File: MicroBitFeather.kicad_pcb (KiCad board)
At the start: 2 copper layers, 67.3 x 35.6 mm, 16 parts, among them J1 Feather_Long, J2 Barrel_Jack_MountingPin, J3 Feather_Short, J4 NeoPixels, J5 microbit_edge_connector, U1 74AHCT125, U2 MCP1702-3302E_TO92

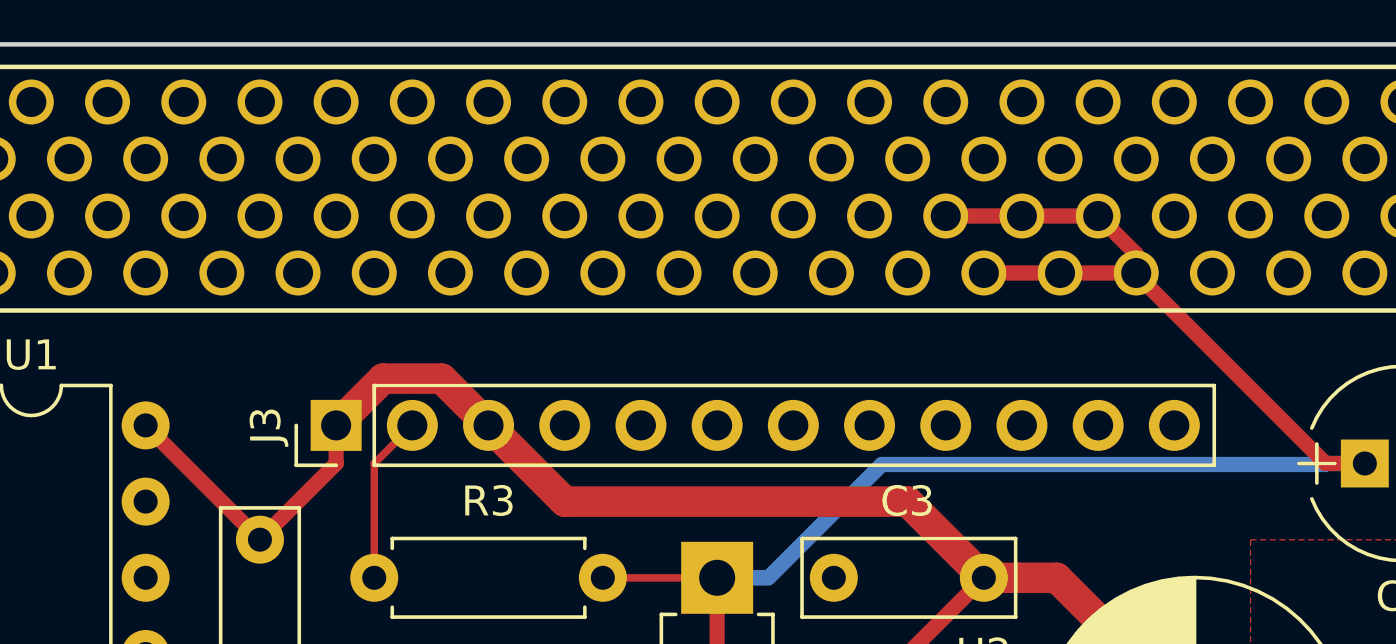
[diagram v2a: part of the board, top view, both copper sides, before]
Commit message: Some more tracks.
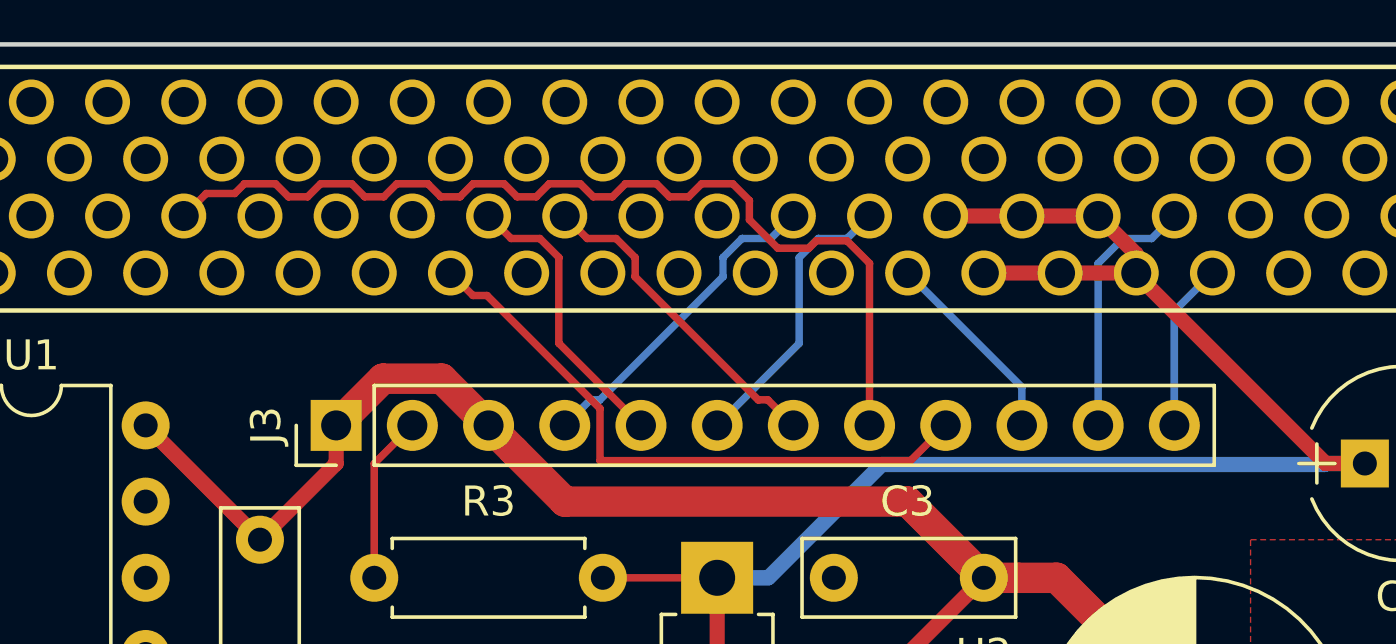
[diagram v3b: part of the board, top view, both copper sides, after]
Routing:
- net /P5: track 0.00 -> 32.6 mm
- net /P8: track 0.00 -> 20.6 mm
- net /SCK: track 0.00 -> 10.9 mm
- net /P11: track 0.00 -> 10.9 mm
- net /P9: track 0.00 -> 9.65 mm
- net /MOSI: track 0.00 -> 9.65 mm
- net /SCL: track 0.00 -> 8.60 mm
- net /P16: track 0.00 -> 6.66 mm
- net /SDA: track 0.00 -> 5.61 mm
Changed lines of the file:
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@@
     (thickness 1.6)
     (drawings 12)
-    (tracks 48)
+    (tracks 122)
     (zones 0)
     (modules 16)
@@
   )
   (setup
-    (last_trace_width 0.508)
+    (last_trace_width 0.25)
     (user_trace_width 0.508)
     (user_trace_width 1.016)
@@
   (segment (start 128.584999 112.885001) (end 125.73 115.74) (width 0.25) (layer F.Cu) (net 5))
   (segment (start 125.73 115.74) (end 125.73 116.84) (width 0.25) (layer F.Cu) (net 5))
+  (segment (start 143.51 96.52) (end 144.359999 95.670001) (width 0.25) (layer B.Cu) (net 13))
+  (segment (start 144.359999 95.670001) (end 144.681001 95.670001) (width 0.25) (layer B.Cu) (net 13))
+  (segment (start 144.681001 95.670001) (end 148.784999 91.566003) (width 0.25) (layer B.Cu) (net 13))
+  (segment (start 148.784999 91.566003) (end 148.784999 90.923999) (width 0.25) (layer B.Cu) (net 13))
+  (segment (start 148.784999 90.923999) (end 149.418999 90.289999) (width 0.25) (layer B.Cu) (net 13))
+  (segment (start 149.418999 90.289999) (end 150.380001 90.289999) (width 0.25) (layer B.Cu) (net 13))
+  (segment (start 150.380001 90.289999) (end 151.13 89.54) (width 0.25) (layer B.Cu) (net 13))
+  (segment (start 148.59 96.52) (end 151.324999 93.785001) (width 0.25) (layer B.Cu) (net 14))
+  (segment (start 151.324999 93.785001) (end 151.324999 90.923999) (width 0.25) (layer B.Cu) (net 14))
+  (segment (start 151.324999 90.923999) (end 151.958999 90.289999) (width 0.25) (layer B.Cu) (net 14))
+  (segment (start 151.958999 90.289999) (end 152.920001 90.289999) (width 0.25) (layer B.Cu) (net 14))
+  (segment (start 152.920001 90.289999) (end 153.67 89.54) (width 0.25) (layer B.Cu) (net 14))
   (segment (start 137.16 101.6) (end 137.16 97.79) (width 0.25) (layer F.Cu) (net 19))
   (segment (start 137.16 97.79) (end 138.43 96.52) (width 0.25) (layer F.Cu) (net 19))
+  (segment (start 146.05 96.52) (end 143.315001 93.785001) (width 0.25) (layer F.Cu) (net 20))
+  (segment (start 143.315001 93.785001) (end 143.315001 90.923999) (width 0.25) (layer F.Cu) (net 20))
+  (segment (start 143.315001 90.923999) (end 142.681001 90.289999) (width 0.25) (layer F.Cu) (net 20))
+  (segment (start 142.681001 90.289999) (end 141.719999 90.289999) (width 0.25) (layer F.Cu) (net 20))
+  (segment (start 141.719999 90.289999) (end 140.97 89.54) (width 0.25) (layer F.Cu) (net 20))
+  (segment (start 151.13 96.52) (end 150.280001 95.670001) (width 0.25) (layer F.Cu) (net 21))
+  (segment (start 150.280001 95.670001) (end 149.958999 95.670001) (width 0.25) (layer F.Cu) (net 21))
+  (segment (start 149.958999 95.670001) (end 145.855001 91.566003) (width 0.25) (layer F.Cu) (net 21))
+  (segment (start 145.855001 91.566003) (end 145.855001 90.923999) (width 0.25) (layer F.Cu) (net 21))
+  (segment (start 145.855001 90.923999) (end 145.221001 90.289999) (width 0.25) (layer F.Cu) (net 21))
+  (segment (start 145.221001 90.289999) (end 144.259999 90.289999) (width 0.25) (layer F.Cu) (net 21))
+  (segment (start 144.259999 90.289999) (end 143.51 89.54) (width 0.25) (layer F.Cu) (net 21))
+  (segment (start 153.67 96.52) (end 153.67 91.118998) (width 0.25) (layer F.Cu) (net 22))
+  (segment (start 153.67 91.118998) (end 152.916001 90.364999) (width 0.25) (layer F.Cu) (net 22))
+  (segment (start 151.896003 90.364999) (end 151.646001 90.615001) (width 0.25) (layer F.Cu) (net 22))
+  (segment (start 151.646001 90.615001) (end 150.613999 90.615001) (width 0.25) (layer F.Cu) (net 22))
+  (segment (start 152.916001 90.364999) (end 151.896003 90.364999) (width 0.25) (layer F.Cu) (net 22))
+  (segment (start 149.665001 89.666003) (end 149.665001 89.023999) (width 0.25) (layer F.Cu) (net 22))
+  (segment (start 150.613999 90.615001) (end 149.665001 89.666003) (width 0.25) (layer F.Cu) (net 22))
+  (segment (start 149.665001 89.023999) (end 149.106001 88.464999) (width 0.25) (layer F.Cu) (net 22))
+  (segment (start 149.106001 88.464999) (end 148.073999 88.464999) (width 0.25) (layer F.Cu) (net 22))
+  (segment (start 147.638998 88.9) (end 147.001002 88.9) (width 0.25) (layer F.Cu) (net 22))
+  (segment (start 148.073999 88.464999) (end 147.638998 88.9) (width 0.25) (layer F.Cu) (net 22))
+  (segment (start 146.566001 88.464999) (end 145.533999 88.464999) (width 0.25) (layer F.Cu) (net 22))
+  (segment (start 145.533999 88.464999) (end 145.098998 88.9) (width 0.25) (layer F.Cu) (net 22))
+  (segment (start 145.098998 88.9) (end 144.461002 88.9) (width 0.25) (layer F.Cu) (net 22))
+  (segment (start 147.001002 88.9) (end 146.566001 88.464999) (width 0.25) (layer F.Cu) (net 22))
+  (segment (start 144.461002 88.9) (end 144.026001 88.464999) (width 0.25) (layer F.Cu) (net 22))
+  (segment (start 144.026001 88.464999) (end 142.993999 88.464999) (width 0.25) (layer F.Cu) (net 22))
+  (segment (start 142.558998 88.9) (end 141.921002 88.9) (width 0.25) (layer F.Cu) (net 22))
+  (segment (start 142.993999 88.464999) (end 142.558998 88.9) (width 0.25) (layer F.Cu) (net 22))
+  (segment (start 141.486001 88.464999) (end 140.453999 88.464999) (width 0.25) (layer F.Cu) (net 22))
+  (segment (start 141.921002 88.9) (end 141.486001 88.464999) (width 0.25) (layer F.Cu) (net 22))
+  (segment (start 140.453999 88.464999) (end 140.018998 88.9) (width 0.25) (layer F.Cu) (net 22))
+  (segment (start 138.946001 88.464999) (end 137.913999 88.464999) (width 0.25) (layer F.Cu) (net 22))
+  (segment (start 139.381002 88.9) (end 138.946001 88.464999) (width 0.25) (layer F.Cu) (net 22))
+  (segment (start 140.018998 88.9) (end 139.381002 88.9) (width 0.25) (layer F.Cu) (net 22))
+  (segment (start 137.913999 88.464999) (end 137.478998 88.9) (width 0.25) (layer F.Cu) (net 22))
+  (segment (start 137.478998 88.9) (end 136.841002 88.9) (width 0.25) (layer F.Cu) (net 22))
+  (segment (start 136.406001 88.464999) (end 135.373999 88.464999) (width 0.25) (layer F.Cu) (net 22))
+  (segment (start 136.841002 88.9) (end 136.406001 88.464999) (width 0.25) (layer F.Cu) (net 22))
+  (segment (start 135.373999 88.464999) (end 134.938998 88.9) (width 0.25) (layer F.Cu) (net 22))
+  (segment (start 134.938998 88.9) (end 134.301002 88.9) (width 0.25) (layer F.Cu) (net 22))
+  (segment (start 134.301002 88.9) (end 133.866001 88.464999) (width 0.25) (layer F.Cu) (net 22))
+  (segment (start 133.866001 88.464999) (end 132.833999 88.464999) (width 0.25) (layer F.Cu) (net 22))
+  (segment (start 132.833999 88.464999) (end 132.508997 88.790001) (width 0.25) (layer F.Cu) (net 22))
+  (segment (start 132.508997 88.790001) (end 131.559999 88.790001) (width 0.25) (layer F.Cu) (net 22))
+  (segment (start 131.559999 88.790001) (end 130.81 89.54) (width 0.25) (layer F.Cu) (net 22))
+  (segment (start 156.21 96.52) (end 155.034999 97.695001) (width 0.25) (layer F.Cu) (net 23))
+  (segment (start 155.034999 97.695001) (end 144.685001 97.695001) (width 0.25) (layer F.Cu) (net 23))
+  (segment (start 144.685001 95.955999) (end 140.919001 92.189999) (width 0.25) (layer F.Cu) (net 23))
+  (segment (start 144.685001 97.695001) (end 144.685001 95.955999) (width 0.25) (layer F.Cu) (net 23))
+  (segment (start 140.919001 92.189999) (end 140.449999 92.189999) (width 0.25) (layer F.Cu) (net 23))
+  (segment (start 140.449999 92.189999) (end 139.7 91.44) (width 0.25) (layer F.Cu) (net 23))
+  (segment (start 158.75 96.52) (end 158.75 95.25) (width 0.25) (layer B.Cu) (net 24))
+  (segment (start 158.75 95.25) (end 154.94 91.44) (width 0.25) (layer B.Cu) (net 24))
+  (segment (start 161.29 96.52) (end 161.29 91.118998) (width 0.25) (layer B.Cu) (net 25))
+  (segment (start 161.29 91.118998) (end 162.118999 90.289999) (width 0.25) (layer B.Cu) (net 25))
+  (segment (start 162.118999 90.289999) (end 163.080001 90.289999) (width 0.25) (layer B.Cu) (net 25))
+  (segment (start 163.080001 90.289999) (end 163.83 89.54) (width 0.25) (layer B.Cu) (net 25))
+  (segment (start 163.83 96.52) (end 163.83 92.71) (width 0.25) (layer B.Cu) (net 26))
+  (segment (start 163.83 92.71) (end 165.1 91.44) (width 0.25) (layer B.Cu) (net 26))
   (zone (net 1) (net_name +5V) (layer F.Cu) (hatch edge 0.508)
     (connect_pads (clearance 0.3048))

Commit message: I meant for NeoPixel pin to be P0.
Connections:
- U1 pad 2: /P1 -> /P0
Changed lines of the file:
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@@
   (general
     (links 79)
-    (no_connects 71)
-    (area 115.424999 71.584999 217.260002 148.48)
+    (no_connects 50)
+    (area 118.034999 83.744999 185.495001 119.455001)
     (thickness 1.6)
     (drawings 12)
@@
       (net 69 "Net-(U1-Pad8)"))
     (pad 2 thru_hole oval (at 0 2.54) (size 1.6 1.6) (drill 0.8) (layers *.Cu *.Mask)
-      (net 8 /P1))
+      (net 7 /P0))
     (pad 9 thru_hole oval (at 7.62 12.7) (size 1.6 1.6) (drill 0.8) (layers *.Cu *.Mask)
       (net 2 GND))

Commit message: More tracks.
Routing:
- net /P3: track 0.00 -> 52.7 mm
- net /P0: track 0.00 -> 51.1 mm
- net /P4: track 0.00 -> 44.1 mm
- net /P2: track 0.00 -> 36.6 mm
- net /P1: track 0.00 -> 35.0 mm
- net /P10: track 0.00 -> 28.3 mm, vias 0 -> 2
- net /MOSI: track 9.65 -> 34.7 mm
- net /SCK: track 10.9 -> 34.8 mm, vias 0 -> 2
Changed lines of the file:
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@@
     (thickness 1.6)
     (drawings 12)
-    (tracks 122)
+    (tracks 196)
     (zones 0)
     (modules 16)
@@
   (segment (start 128.584999 112.885001) (end 125.73 115.74) (width 0.25) (layer F.Cu) (net 5))
   (segment (start 125.73 115.74) (end 125.73 116.84) (width 0.25) (layer F.Cu) (net 5))
+  (segment (start 124.46 91.44) (end 124.46 90.81) (width 0.25) (layer B.Cu) (net 7))
+  (segment (start 124.46 90.81) (end 125.73 89.54) (width 0.25) (layer B.Cu) (net 7))
+  (segment (start 127 91.44) (end 127 90.81) (width 0.25) (layer B.Cu) (net 7))
+  (segment (start 127 90.81) (end 128.27 89.54) (width 0.25) (layer B.Cu) (net 7))
+  (segment (start 124.46 91.44) (end 127 91.44) (width 0.25) (layer B.Cu) (net 7))
+  (segment (start 120.65 97.79) (end 120.65 95.25) (width 0.25) (layer B.Cu) (net 7))
+  (segment (start 120.65 95.25) (end 124.46 91.44) (width 0.25) (layer B.Cu) (net 7))
+  (segment (start 121.92 99.06) (end 120.65 97.79) (width 0.25) (layer B.Cu) (net 7))
+  (segment (start 119.38 112.775002) (end 119.38 101.6) (width 0.25) (layer F.Cu) (net 7))
+  (segment (start 119.38 101.6) (end 121.92 99.06) (width 0.25) (layer F.Cu) (net 7))
+  (segment (start 135.89 116.84) (end 134.714999 118.015001) (width 0.25) (layer F.Cu) (net 7))
+  (segment (start 134.714999 118.015001) (end 124.619999 118.015001) (width 0.25) (layer F.Cu) (net 7))
+  (segment (start 124.619999 118.015001) (end 119.38 112.775002) (width 0.25) (layer F.Cu) (net 7))
+  (segment (start 137.16 91.44) (end 134.62 91.44) (width 0.25) (layer B.Cu) (net 8))
+  (segment (start 138.43 89.54) (end 137.680001 88.790001) (width 0.25) (layer B.Cu) (net 8))
+  (segment (start 137.680001 88.790001) (end 136.639999 88.790001) (width 0.25) (layer B.Cu) (net 8))
+  (segment (start 136.639999 88.790001) (end 135.89 89.54) (width 0.25) (layer B.Cu) (net 8))
+  (segment (start 137.16 91.44) (end 137.16 90.81) (width 0.25) (layer B.Cu) (net 8))
+  (segment (start 137.16 90.81) (end 138.43 89.54) (width 0.25) (layer B.Cu) (net 8))
+  (segment (start 138.43 116.84) (end 139.605001 115.664999) (width 0.25) (layer B.Cu) (net 8))
+  (segment (start 139.605001 115.664999) (end 139.605001 93.885001) (width 0.25) (layer B.Cu) (net 8))
+  (segment (start 139.605001 93.885001) (end 137.909999 92.189999) (width 0.25) (layer B.Cu) (net 8))
+  (segment (start 137.909999 92.189999) (end 137.16 91.44) (width 0.25) (layer B.Cu) (net 8))
+  (segment (start 148.59 89.54) (end 147.52934 89.54) (width 0.25) (layer F.Cu) (net 9))
+  (segment (start 147.52934 89.54) (end 146.05 89.54) (width 0.25) (layer F.Cu) (net 9))
+  (segment (start 149.86 91.44) (end 149.86 90.81) (width 0.25) (layer F.Cu) (net 9))
+  (segment (start 149.86 90.81) (end 148.59 89.54) (width 0.25) (layer F.Cu) (net 9))
+  (segment (start 149.86 91.44) (end 147.32 91.44) (width 0.25) (layer F.Cu) (net 9))
+  (segment (start 140.97 116.84) (end 140.97 103.744998) (width 0.25) (layer B.Cu) (net 9))
+  (segment (start 140.97 103.744998) (end 147.414999 97.299999) (width 0.25) (layer B.Cu) (net 9))
+  (segment (start 147.414999 93.885001) (end 149.110001 92.189999) (width 0.25) (layer B.Cu) (net 9))
+  (segment (start 147.414999 97.299999) (end 147.414999 93.885001) (width 0.25) (layer B.Cu) (net 9))
+  (segment (start 149.110001 92.189999) (end 149.86 91.44) (width 0.25) (layer B.Cu) (net 9))
+  (segment (start 143.51 116.84) (end 141.884989 118.465011) (width 0.25) (layer F.Cu) (net 10))
+  (segment (start 141.884989 118.465011) (end 124.433598 118.46501) (width 0.25) (layer F.Cu) (net 10))
+  (segment (start 118.92999 112.961402) (end 118.92999 93.80001) (width 0.25) (layer F.Cu) (net 10))
+  (segment (start 124.433598 118.46501) (end 118.92999 112.961402) (width 0.25) (layer F.Cu) (net 10))
+  (segment (start 118.92999 93.80001) (end 122.440001 90.289999) (width 0.25) (layer F.Cu) (net 10))
+  (segment (start 122.440001 90.289999) (end 123.19 89.54) (width 0.25) (layer F.Cu) (net 10))
+  (segment (start 129.54 91.44) (end 128.414999 92.565001) (width 0.25) (layer B.Cu) (net 11))
+  (segment (start 128.414999 92.565001) (end 128.414999 115.245997) (width 0.25) (layer B.Cu) (net 11))
+  (segment (start 128.414999 115.245997) (end 129.634999 116.465997) (width 0.25) (layer B.Cu) (net 11))
+  (segment (start 129.634999 116.465997) (end 129.634999 117.404001) (width 0.25) (layer B.Cu) (net 11))
+  (segment (start 129.634999 117.404001) (end 130.245999 118.015001) (width 0.25) (layer B.Cu) (net 11))
+  (segment (start 130.245999 118.015001) (end 144.874999 118.015001) (width 0.25) (layer B.Cu) (net 11))
+  (segment (start 144.874999 118.015001) (end 145.200001 117.689999) (width 0.25) (layer B.Cu) (net 11))
+  (segment (start 145.200001 117.689999) (end 146.05 116.84) (width 0.25) (layer B.Cu) (net 11))
+  (segment (start 142.24 104.14) (end 142.24 110.885002) (width 0.25) (layer B.Cu) (net 12))
+  (segment (start 142.24 110.885002) (end 147.344999 115.990001) (width 0.25) (layer B.Cu) (net 12))
+  (segment (start 147.344999 115.990001) (end 147.740001 115.990001) (width 0.25) (layer B.Cu) (net 12))
+  (segment (start 147.740001 115.990001) (end 148.59 116.84) (width 0.25) (layer B.Cu) (net 12))
+  (segment (start 142.235557 101.595557) (end 142.235557 104.135557) (width 0.25) (layer F.Cu) (net 12))
+  (segment (start 142.235557 104.135557) (end 142.24 104.14) (width 0.25) (layer F.Cu) (net 12))
+  (via (at 142.24 104.14) (size 0.6) (drill 0.4) (layers F.Cu B.Cu) (net 12))
+  (segment (start 142.24 91.44) (end 142.24 101.591114) (width 0.25) (layer B.Cu) (net 12))
+  (segment (start 142.24 101.591114) (end 142.235557 101.595557) (width 0.25) (layer B.Cu) (net 12))
+  (via (at 142.235557 101.595557) (size 0.6) (drill 0.4) (layers F.Cu B.Cu) (net 12))
+  (segment (start 143.505557 100.325557) (end 143.505557 96.524443) (width 0.25) (layer B.Cu) (net 13))
+  (segment (start 143.505557 96.524443) (end 143.51 96.52) (width 0.25) (layer B.Cu) (net 13))
+  (segment (start 143.51 104.14) (end 143.51 100.33) (width 0.25) (layer F.Cu) (net 13))
+  (segment (start 143.51 100.33) (end 143.505557 100.325557) (width 0.25) (layer F.Cu) (net 13))
+  (via (at 143.505557 100.325557) (size 0.6) (drill 0.4) (layers F.Cu B.Cu) (net 13))
+  (segment (start 151.13 116.84) (end 150.776588 116.84) (width 0.25) (layer B.Cu) (net 13))
+  (segment (start 150.776588 116.84) (end 145.905001 111.968413) (width 0.25) (layer B.Cu) (net 13))
+  (segment (start 145.905001 111.968413) (end 145.905001 106.139999) (width 0.25) (layer B.Cu) (net 13))
+  (segment (start 145.905001 106.139999) (end 143.905002 104.14) (width 0.25) (layer B.Cu) (net 13))
+  (segment (start 143.905002 104.14) (end 143.51 104.14) (width 0.25) (layer B.Cu) (net 13))
+  (via (at 143.51 104.14) (size 0.6) (drill 0.4) (layers F.Cu B.Cu) (net 13))
   (segment (start 143.51 96.52) (end 144.359999 95.670001) (width 0.25) (layer B.Cu) (net 13))
   (segment (start 144.359999 95.670001) (end 144.681001 95.670001) (width 0.25) (layer B.Cu) (net 13))
@@
   (segment (start 149.418999 90.289999) (end 150.380001 90.289999) (width 0.25) (layer B.Cu) (net 13))
   (segment (start 150.380001 90.289999) (end 151.13 89.54) (width 0.25) (layer B.Cu) (net 13))
+  (segment (start 153.67 116.84) (end 152.494999 115.664999) (width 0.25) (layer B.Cu) (net 14))
+  (segment (start 152.494999 115.664999) (end 150.237997 115.664999) (width 0.25) (layer B.Cu) (net 14))
+  (segment (start 150.237997 115.664999) (end 147.064999 112.492001) (width 0.25) (layer B.Cu) (net 14))
+  (segment (start 147.064999 112.492001) (end 147.064999 99.247082) (width 0.25) (layer B.Cu) (net 14))
+  (segment (start 147.064999 99.247082) (end 148.59 97.722081) (width 0.25) (layer B.Cu) (net 14))
+  (segment (start 148.59 97.722081) (end 148.59 96.52) (width 0.25) (layer B.Cu) (net 14))
   (segment (start 148.59 96.52) (end 151.324999 93.785001) (width 0.25) (layer B.Cu) (net 14))
   (segment (start 151.324999 93.785001) (end 151.324999 90.923999) (width 0.25) (layer B.Cu) (net 14))
